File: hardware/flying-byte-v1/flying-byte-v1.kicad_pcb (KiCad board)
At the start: 4 copper layers, 0 parts

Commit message: feat: Add the net classes colors and initialize pcb with parts
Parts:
- added C1: 4u7, Capacitor_SMD:C_0603_1608Metric, F.Cu at (142.5, 90.8)
- added C10: 4u7, Capacitor_SMD:C_0603_1608Metric, F.Cu at (142.5, 98.4)
- added C11: 100n, Capacitor_SMD:C_0402_1005Metric, F.Cu at (129.7, 96.7)
- added C12: 100n, Capacitor_SMD:C_0402_1005Metric, F.Cu at (129.7, 98.7)
- added C13: 100n, Capacitor_SMD:C_0402_1005Metric, F.Cu at (129.7, 100.6)
- added C14: 4u7, Capacitor_SMD:C_0603_1608Metric, F.Cu at (142.5, 100.9)
- added C15: 0p8, Capacitor_SMD:C_0402_1005Metric, F.Cu at (129.7, 102.6)
- added C16: 0p3, Capacitor_SMD:C_0402_1005Metric, F.Cu at (132.6, 94.7)
- added C17: 10p, Capacitor_SMD:C_0402_1005Metric, F.Cu at (132.6, 96.7)
- added C18: 10p, Capacitor_SMD:C_0402_1005Metric, F.Cu at (132.6, 98.7)
- added C19: 100n, Capacitor_SMD:C_0402_1005Metric, F.Cu at (132.6, 100.6)
- added C2: 4u7, Capacitor_SMD:C_0603_1608Metric, F.Cu at (142.5, 93.3)
- added C3: 4u7, Capacitor_SMD:C_0603_1608Metric, F.Cu at (142.5, 95.9)
- added C4: 100n, Capacitor_SMD:C_0402_1005Metric, F.Cu at (126.8, 94.7)
- added C5: 100n, Capacitor_SMD:C_0402_1005Metric, F.Cu at (126.8, 96.7)
- added C6: 100n, Capacitor_SMD:C_0402_1005Metric, F.Cu at (126.8, 98.7)
- added C7: 100n, Capacitor_SMD:C_0402_1005Metric, F.Cu at (126.8, 100.6)
- added C8: 100n, Capacitor_SMD:C_0402_1005Metric, F.Cu at (126.8, 102.6)
- added C9: 100n, Capacitor_SMD:C_0402_1005Metric, F.Cu at (129.7, 94.7)
- added D1: LED, LED_SMD:LED_0402_1005Metric, F.Cu at (151.6, 95.8)
- added D2: LED, LED_SMD:LED_0402_1005Metric, F.Cu at (151.6, 97.8)
- added FLT1: DLF162500LT-5028A1, flying-byte-v1-pcb-footprints:DLF162500LT-5028A1, F.Cu at (146.3, 102.0)
- added J1: Conn_Coaxial, Connector_Coaxial:U.FL_Hirose_U.FL-R-SMT-1_Vertical, F.Cu at (147.1, 97.9)
- added J2: Conn_ARM_SWD_TagConnect_TC2030, Connector:Tag-Connect_TC2030-IDC-FP_2x03_P1.27mm_Vertical, F.Cu at (141.9, 79.2)
- added J3: USB_C_Receptacle_USB2.0, Connector_USB:USB_C_Receptacle_GCT_USB4105-xx-A_16P_TopMnt_Horizontal, F.Cu at (131.3, 79.7)
- added J4: Conn_01x04, Connector_Molex:Molex_PicoBlade_53047-0410_1x04_P1.25mm_Vertical, F.Cu at (147.1, 92.7)
- added L1: 10n, Inductor_SMD:L_0402_1005Metric, F.Cu at (136.2, 85.4)
- added L2: 10u, Inductor_SMD:L_0805_2012Metric, F.Cu at (137.0, 101.4)
- added L3: 2n7, Inductor_SMD:L_0402_1005Metric, F.Cu at (136.2, 87.4)
- added R1: 220R, Resistor_SMD:R_0402_1005Metric, F.Cu at (136.2, 89.4)
- added R2: 220R, Resistor_SMD:R_0402_1005Metric, F.Cu at (136.2, 91.4)
- added R3: 220R, Resistor_SMD:R_0402_1005Metric, F.Cu at (136.2, 93.4)
- added R4: 220R, Resistor_SMD:R_0402_1005Metric, F.Cu at (136.2, 95.4)
- added R5: 5k1, Resistor_SMD:R_0402_1005Metric, F.Cu at (139.1, 85.4)
- added R6: 5k1, Resistor_SMD:R_0402_1005Metric, F.Cu at (139.1, 87.4)
- added R7: 0, Resistor_SMD:R_0402_1005Metric, F.Cu at (139.1, 89.4)
- added R8: 5k1, Resistor_SMD:R_0402_1005Metric, F.Cu at (139.1, 91.4)
- added R9: 220R, Resistor_SMD:R_0402_1005Metric, F.Cu at (139.1, 93.4)
- added SW1: SW_Push, Button_Switch_SMD:SW_SPST_CK_RS282G05A3, F.Cu at (145.9, 87.0)
- added U1: STM32WB55CEU6, Package_DFN_QFN:QFN-48-1EP_7x7mm_P0.5mm_EP5.6x5.6mm, F.Cu at (130.1, 89.1)
- added U2: USBLC6-2SC6_MOD, Package_TO_SOT_SMD:SOT-23-6, F.Cu at (148.7, 76.7)
- added U3: MIC5365-3.3YD5, Package_TO_SOT_SMD:SOT-23-5, F.Cu at (148.7, 81.1)
- added X1: 32MHz, Crystal:Crystal_SMD_2016-4Pin_2.0x1.6mm, F.Cu at (136.6, 98.2)
- added X2: 32kHz768, Crystal:Crystal_SMD_2012-2Pin_2.0x1.2mm, F.Cu at (151.7, 100.2)

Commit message: feat: Add the initial layout
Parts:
- J4: footprint Connector_Molex:Molex_PicoBlade_53047-0410_1x04_P1.25mm_Vertical -> Connector_Molex:Molex_PicoBlade_53048-0410_1x04_P1.25mm_Horizontal
- moved J4 49.3 mm to (97.9, 96.6), turned to -90 degrees
- moved D1 44.4 mm to (107.3, 99.0)
- moved U3 44.0 mm to (106.8, 94.5), turned to -90 degrees
- moved U2 43.3 mm to (106.8, 87.4)
- moved R5 42.6 mm to (97.2, 93.4), turned to 180 degrees
- moved R6 42.3 mm to (97.2, 81.3), turned to 180 degrees
- moved C2 36.0 mm to (106.8, 97.5), turned to 180 degrees
- moved C1 35.7 mm to (106.8, 91.5), turned to 180 degrees
- moved J3 34.9 mm to (97.2, 87.3), turned to -90 degrees
- moved R1 30.8 mm to (107.3, 100.2), turned to 180 degrees
- moved J2 28.4 mm to (115.3, 89.1), turned to -90 degrees
- moved X2 26.3 mm to (125.7, 96.0), turned to 180 degrees
- moved C10 25.2 mm to (123.8, 81.5), turned to 180 degrees
- moved SW1 23.4 mm to (126.4, 100.0)
- moved C14 22.4 mm to (128.5, 83.4)
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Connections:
- net Net-(C17-Pad1) renamed /LSE_OUT_R
- net Net-(J4-Pin_2) renamed /UART_RXC
- net Net-(J4-Pin_3) renamed /UART_TXC
- net Net-(R9-Pad2) renamed /BOOT0_SW

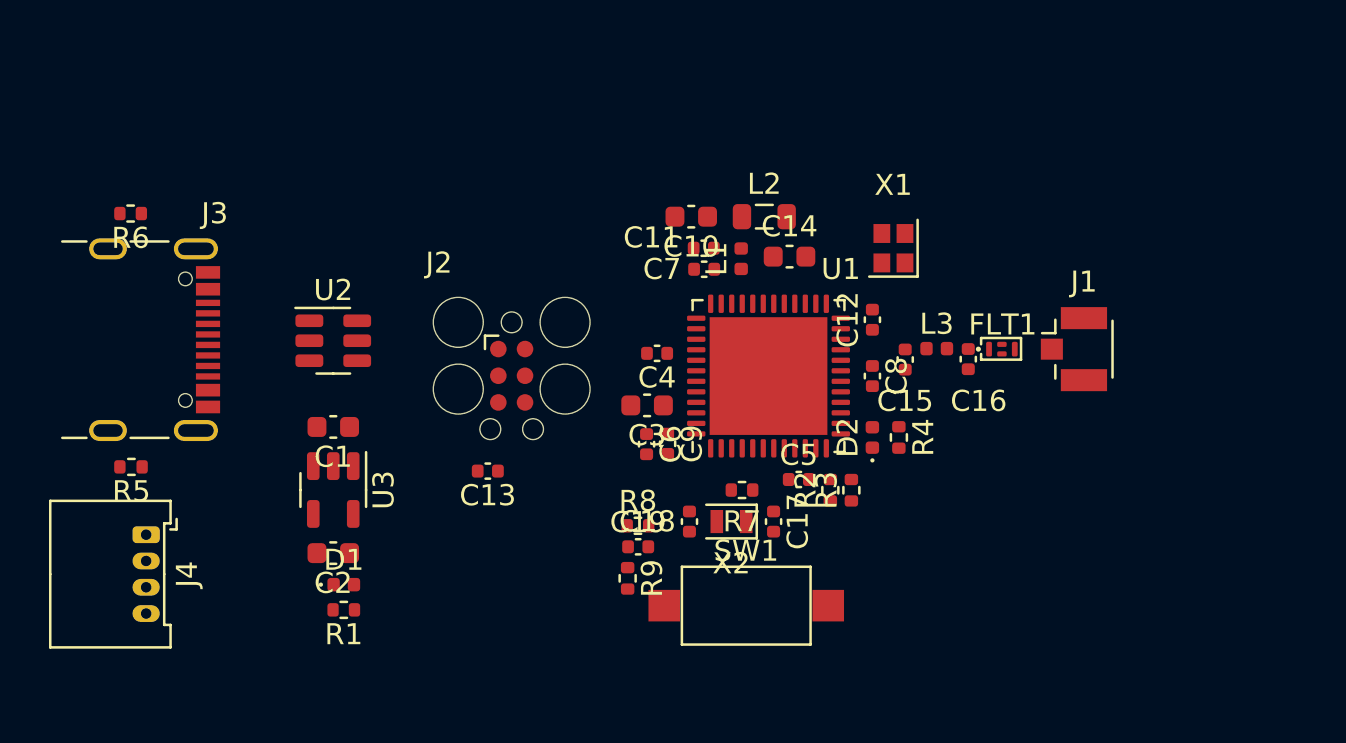
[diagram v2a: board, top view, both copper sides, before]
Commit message: feat: Add outline, mounting holes and fiducial markers
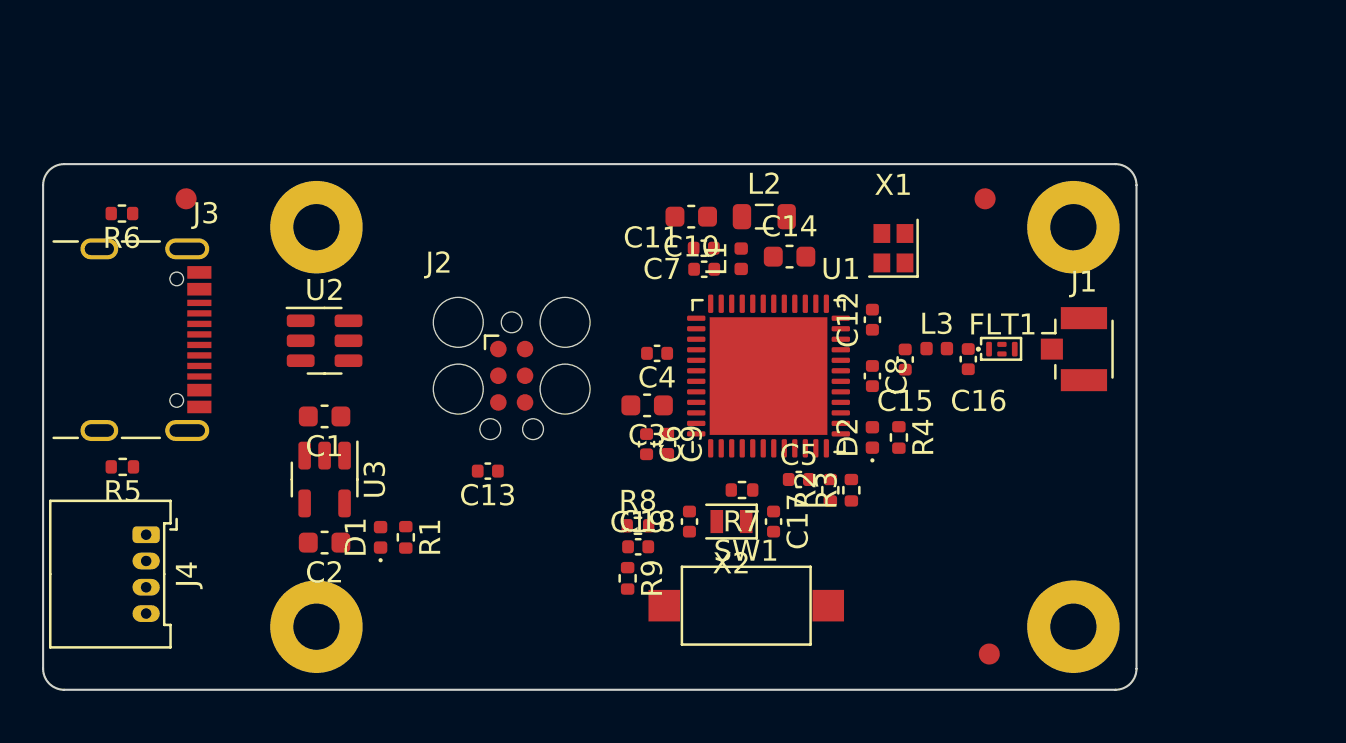
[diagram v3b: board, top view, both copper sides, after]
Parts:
- added FM1: Fiducial, Fiducial:Fiducial_1mm_Mask2mm, F.Cu at (138.0, 102.3)
- added FM2: Fiducial, Fiducial:Fiducial_1mm_Mask2mm, F.Cu at (137.8, 80.7)
- added FM3: Fiducial, Fiducial:Fiducial_1mm_Mask2mm, F.Cu at (99.8, 80.7)
- added H1: MountingHole_Pad, MountingHole:MountingHole_2.2mm_M2_Pad, F.Cu at (142.0, 82.0)
- added H2: MountingHole_Pad, MountingHole:MountingHole_2.2mm_M2_Pad, F.Cu at (142.0, 101.0)
- added H3: MountingHole_Pad, MountingHole:MountingHole_2.2mm_M2_Pad, F.Cu at (106.0, 82.0)
- added H4: MountingHole_Pad, MountingHole:MountingHole_2.2mm_M2_Pad, F.Cu at (106.0, 101.0)
- moved R1 4.54 mm to (110.2, 96.8), turned to -90 degrees
- moved D1 2.85 mm to (109.0, 96.8), turned to 90 degrees
- moved C1 0.65 mm to (106.4, 91.0)
- moved C2 0.65 mm to (106.4, 97.0)
- moved U3 0.65 mm to (106.4, 94.0)
- moved R5 0.41 mm to (96.8, 93.4)
- moved J3 0.41 mm to (96.8, 87.3)
- moved R6 0.41 mm to (96.8, 81.3)
- moved U2 0.41 mm to (106.4, 87.4)
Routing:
- added copper zone on In1.Cu, net GND
- added copper zone on In2.Cu, net GND
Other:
- board outline added: 52 x 25 mm

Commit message: feat: PCB routing #1
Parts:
- moved C19 12.7 mm to (133.1, 102.0)
- moved R8 12.7 mm to (133.1, 101.0)
- moved R9 11.1 mm to (131.5, 101.5), turned to 90 degrees
- moved R2 0.93 mm to (129.5, 94.3)
- moved R3 0.93 mm to (130.5, 94.3)
- moved C5 0.67 mm to (128.3, 94.3), turned to -90 degrees
- moved C17 0.64 mm to (127.2, 96.4)
- moved C18 0.64 mm to (123.2, 96.4)
- moved R7 0.64 mm to (125.7, 94.9)
- moved X2 0.64 mm to (125.2, 96.4)
- moved C4 0.60 mm to (121.6, 88.1)
- moved SW1 0.60 mm to (125.9, 100.2), turned to 180 degrees
- moved C13 0.29 mm to (113.9, 93.6)
- moved J2 0.28 mm to (115.0, 89.1)
- moved C12 0.16 mm to (132.6, 86.4)
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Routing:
- net /USB_D-: track 0.00 -> 16.8 mm
- net /USB_D+: track 0.00 -> 16.4 mm
- net /SWD_NRST: track 0.00 -> 15.9 mm, vias 0 -> 2
- net /BOOT0: track 0.00 -> 14.8 mm, vias 0 -> 2
- net /SWD_DIO: track 0.00 -> 12.0 mm
- net /SWD_TRC: track 0.00 -> 10.3 mm
- net /SWD_CLK: track 0.00 -> 9.29 mm
- net /LSE_IN: track 0.00 -> 5.65 mm
- net /HSE_OUT: track 0.00 -> 5.21 mm
- net /HSE_IN: track 0.00 -> 5.06 mm
- net /RF: track 0.00 -> 4.10 mm
- net /LSE_OUT_R: track 0.00 -> 3.13 mm
- net /LSE_OUT: track 0.00 -> 2.57 mm
- net /RF_MATCH: track 0.00 -> 2.03 mm
- net /RF_ANT: track 0.00 -> 1.76 mm
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- added copper zone on F.Cu, net /SMPS_VFB

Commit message: feat: PCB routing #2
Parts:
- turned U2 to 0 degrees
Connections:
- U2 pad 1: /USBC_D+ -> /USBC_D-
- U2 pad 3: /USBC_D- -> /USBC_D+
- U2 pad 4: /USB_D- -> /USB_D+
- U2 pad 6: /USB_D+ -> /USB_D-
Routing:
- net /USBC_D+: track 0.00 -> 8.59 mm
- net /USBC_D-: track 0.00 -> 8.10 mm
- net /USBC_CC1: track 0.00 -> 6.84 mm
- net /USBC_CC2: track 0.00 -> 6.38 mm
- net /USB_D+: track 16.4 -> 21.4 mm
- net /USB_D-: track 16.8 -> 20.7 mm
- net GND: vias 37 -> 39
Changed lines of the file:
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@@
   )
   (footprint "Package_TO_SOT_SMD:SOT-23-6" (layer "F.Cu")
-    (at 106.3875 87.4 180)
+    (at 106.3875 87.4)
     (descr "SOT, 6 Pin (https://www.jedec.org/sites/default/files/docs/Mo-178c.PDF variant AB), generated with kicad-footprint-generator ipc_gullwing_generator.py")
     (tags "SOT TO_SOT_SMD")
@@
     (fp_line (start 0.8 1.45) (end -0.8 1.45)
       (stroke (width 0.1) (type solid)) (layer "F.Fab"))
-    (pad "1" smd roundrect (at -1.1375 -0.95 180) (size 1.325 0.6) (layers "F.Cu" "F.Paste" "F.Mask") (roundrect_rratio 0.25)
+    (pad "1" smd roundrect (at -1.1375 -0.95) (size 1.325 0.6) (layers "F.Cu" "F.Paste" "F.Mask") (roundrect_rratio 0.25)
+      (net 20 "/USBC_D-") (pinfunction "I/O1") (pintype "passive"))
+    (pad "2" smd roundrect (at -1.1375 0) (size 1.325 0.6) (layers "F.Cu" "F.Paste" "F.Mask") (roundrect_rratio 0.25)
+      (net 2 "GND") (pinfunction "GND") (pintype "passive"))
+    (pad "3" smd roundrect (at -1.1375 0.95) (size 1.325 0.6) (layers "F.Cu" "F.Paste" "F.Mask") (roundrect_rratio 0.25)
       (net 19 "/USBC_D+") (pinfunction "I/O1") (pintype "passive"))
-    (pad "2" smd roundrect (at -1.1375 0 180) (size 1.325 0.6) (layers "F.Cu" "F.Paste" "F.Mask") (roundrect_rratio 0.25)
-      (net 2 "GND") (pinfunction "GND") (pintype "passive"))
-    (pad "3" smd roundrect (at -1.1375 0.95 180) (size 1.325 0.6) (layers "F.Cu" "F.Paste" "F.Mask") (roundrect_rratio 0.25)
-      (net 20 "/USBC_D-") (pinfunction "I/O1") (pintype "passive"))
-    (pad "4" smd roundrect (at 1.1375 0.95 180) (size 1.325 0.6) (layers "F.Cu" "F.Paste" "F.Mask") (roundrect_rratio 0.25)
+    (pad "4" smd roundrect (at 1.1375 0.95) (size 1.325 0.6) (layers "F.Cu" "F.Paste" "F.Mask") (roundrect_rratio 0.25)
+      (net 51 "/USB_D+") (pinfunction "I/O2") (pintype "passive"))
+    (pad "5" smd roundrect (at 1.1375 0) (size 1.325 0.6) (layers "F.Cu" "F.Paste" "F.Mask") (roundrect_rratio 0.25)
+      (net 1 "+5V") (pinfunction "VBUS") (pintype "passive"))
+    (pad "6" smd roundrect (at 1.1375 -0.95) (size 1.325 0.6) (layers "F.Cu" "F.Paste" "F.Mask") (roundrect_rratio 0.25)
       (net 50 "/USB_D-") (pinfunction "I/O2") (pintype "passive"))
-    (pad "5" smd roundrect (at 1.1375 0 180) (size 1.325 0.6) (layers "F.Cu" "F.Paste" "F.Mask") (roundrect_rratio 0.25)
-      (net 1 "+5V") (pinfunction "VBUS") (pintype "passive"))
-    (pad "6" smd roundrect (at 1.1375 -0.95 180) (size 1.325 0.6) (layers "F.Cu" "F.Paste" "F.Mask") (roundrect_rratio 0.25)
-      (net 51 "/USB_D+") (pinfunction "I/O2") (pintype "passive"))
     (model "${KICAD6_3DMODEL_DIR}/Package_TO_SOT_SMD.3dshapes/SOT-23-6.wrl"
       (offset (xyz 0 0 0))
@@
   (via (at 142.5 85) (size 0.7) (drill 0.3) (layers "F.Cu" "B.Cu") (free) (net 2))
   (via (at 104.45 91.45) (size 0.7) (drill 0.3) (layers "F.Cu" "B.Cu") (free) (net 2))
+  (via (at 103.91 87.4) (size 0.7) (drill 0.3) (layers "F.Cu" "B.Cu") (free) (net 2))
   (via (at 127.22 97.71) (size 0.7) (drill 0.3) (layers "F.Cu" "B.Cu") (free) (net 2))
   (via (at 131.86 83.9) (size 0.7) (drill 0.3) (layers "F.Cu" "B.Cu") (free) (net 2))
@@
   (via (at 110.25 95.35) (size 0.7) (drill 0.3) (layers "F.Cu" "B.Cu") (free) (net 2))
   (via (at 121.8 82) (size 0.7) (drill 0.3) (layers "F.Cu" "B.Cu") (free) (net 2))
+  (via (at 133.5 93.8) (size 0.7) (drill 0.3) (layers "F.Cu" "B.Cu") (free) (net 2))
   (via (at 142.5 90.6) (size 0.7) (drill 0.3) (layers "F.Cu" "B.Cu") (free) (net 2))
   (via (at 123 83) (size 0.7) (drill 0.3) (layers "F.Cu" "B.Cu") (free) (net 2))
@@
   (segment (start 118.275 91.425) (end 117.025 91.425) (width 0.17) (layer "F.Cu") (net 17))
   (segment (start 119.455 89.33) (end 119.45 89.325) (width 0.17) (layer "F.Cu") (net 17))
+  (segment (start 99.1 86.1) (end 97.26 84.26) (width 0.25) (layer "F.Cu") (net 18))
+  (segment (start 97.26 84.26) (end 97.26 81.35) (width 0.25) (layer "F.Cu") (net 18))
+  (segment (start 100.43 86.1) (end 99.1 86.1) (width 0.25) (layer "F.Cu") (net 18))
+  (segment (start 100.43 87.1) (end 101.292501 87.1) (width 0.22) (layer "F.Cu") (net 19))
+  (segment (start 103.81 88.35) (end 105.25 88.35) (width 0.22) (layer "F.Cu") (net 19))
+  (segment (start 102.978456 88.1) (end 103.169228 87.909228) (width 0.22) (layer "F.Cu") (net 19))
+  (segment (start 101.342501 87.05) (end 102.624228 87.05) (width 0.22) (layer "F.Cu") (net 19))
+  (segment (start 102.624228 87.05) (end 103.169228 87.595) (width 0.22) (layer "F.Cu") (net 19))
+  (segment (start 103.169228 87.595) (end 103.169228 87.909228) (width 0.22) (layer "F.Cu") (net 19))
+  (segment (start 101.292501 87.1) (end 101.342501 87.05) (width 0.22) (layer "F.Cu") (net 19))
+  (segment (start 102.978456 88.1) (end 103.094228 87.984228) (width 0.22) (layer "F.Cu") (net 19))
+  (segment (start 103.094228 87.984228) (end 103.444228 87.984228) (width 0.22) (layer "F.Cu") (net 19))
+  (segment (start 100.43 88.1) (end 102.978456 88.1) (width 0.22) (layer "F.Cu") (net 19))
+  (segment (start 103.444228 87.984228) (end 103.81 88.35) (width 0.22) (layer "F.Cu") (net 19))
+  (segment (start 100.43 86.6) (end 101.292501 86.6) (width 0.22) (layer "F.Cu") (net 20))
+  (segment (start 101.292501 86.6) (end 101.352501 86.66) (width 0.22) (layer "F.Cu") (net 20))
+  (segment (start 102.765772 86.66) (end 102.975772 86.45) (width 0.22) (layer "F.Cu") (net 20))
+  (segment (start 102.975772 86.45) (end 105.25 86.45) (width 0.22) (layer "F.Cu") (net 20))
+  (segment (start 99.23 87.4) (end 99.23 86.8) (width 0.22) (layer "F.Cu") (net 20))
+  (segment (start 99.43 86.6) (end 100.43 86.6) (width 0.22) (layer "F.Cu") (net 20))
+  (segment (start 100.43 87.6) (end 99.43 87.6) (width 0.22) (layer "F.Cu") (net 20))
+  (segment (start 101.352501 86.66) (end 102.765772 86.66) (width 0.22) (layer "F.Cu") (net 20))
+  (segment (start 99.43 87.6) (end 99.23 87.4) (width 0.22) (layer "F.Cu") (net 20))
+  (segment (start 99.23 86.8) (end 99.43 86.6) (width 0.22) (layer "F.Cu") (net 20))
+  (segment (start 100.43 89.1) (end 99.1 89.1) (width 0.25) (layer "F.Cu") (net 22))
+  (segment (start 97.2975 90.9025) (end 97.2975 93.4) (width 0.25) (layer "F.Cu") (net 22))
+  (segment (start 99.1 89.1) (end 97.2975 90.9025) (width 0.25) (layer "F.Cu") (net 22))
   (segment (start 126.25 84.675) (end 126.25 83.985) (width 0.5) (layer "F.Cu") (net 26))
   (segment (start 126.25 85.6425) (end 126.25 84.85) (width 0.25) (layer "F.Cu") (net 26))
@@
   (segment (start 131.2 83.2) (end 131.2 84.1) (width 0.17) (layer "F.Cu") (net 43))
   (segment (start 132.1 82.3) (end 131.2 83.2) (width 0.17) (layer "F.Cu") (net 43))
-  (segment (start 122.860772 86.385) (end 119.560772 83.085) (width 0.22) (layer "F.Cu") (net 50))
-  (segment (start 123.406249 86.33) (end 123.351249 86.385) (width 0.22) (layer "F.Cu") (net 50))
-  (segment (start 110.619228 83.085) (end 109.262114 84.442114) (width 0.22) (layer "F.Cu") (net 50))
+  (segment (start 119.560772 83.085) (end 110.619228 83.085) (width 0.22) (layer "F.Cu") (net 50))
+  (segment (start 110.619228 83.085) (end 109.904888 83.79934) (width 0.22) (layer "F.Cu") (net 50))
+  (segment (start 109.524228 86.45) (end 107.525 86.45) (width 0.22) (layer "F.Cu") (net 50))
+  (segment (start 109.904888 83.79934) (end 109.904888 86.06934) (width 0.22) (layer "F.Cu") (net 50))
+  (segment (start 109.904888 86.06934) (end 109.524228 86.45) (width 0.22) (layer "F.Cu") (net 50))
   (segment (start 123.351249 86.385) (end 122.860772 86.385) (width 0.22) (layer "F.Cu") (net 50))
   (segment (start 124.0625 86.33) (end 123.406249 86.33) (width 0.22) (layer "F.Cu") (net 50))
-  (segment (start 119.560772 83.085) (end 110.619228 83.085) (width 0.22) (layer "F.Cu") (net 50))
+  (segment (start 123.406249 86.33) (end 123.351249 86.385) (width 0.22) (layer "F.Cu") (net 50))
+  (segment (start 122.860772 86.385) (end 119.560772 83.085) (width 0.22) (layer "F.Cu") (net 50))
+  (segment (start 108.45 88.35) (end 107.525 88.35) (width 0.22) (layer "F.Cu") (net 51))
   (segment (start 119.399228 83.475) (end 110.780772 83.475) (width 0.22) (layer "F.Cu") (net 51))
+  (segment (start 110.294888 83.960884) (end 110.294888 86.505112) (width 0.22) (layer "F.Cu") (net 51))
+  (segment (start 123.351249 86.775) (end 122.699228 86.775) (width 0.22) (layer "F.Cu") (net 51))
+  (segment (start 110.294888 86.505112) (end 108.45 88.35) (width 0.22) (layer "F.Cu") (net 51))
+  (segment (start 110.780772 83.475) (end 110.294888 83.960884) (width 0.22) (layer "F.Cu") (net 51))
   (segment (start 123.406249 86.83) (end 123.351249 86.775) (width 0.22) (layer "F.Cu") (net 51))
-  (segment (start 123.351249 86.775) (end 122.699228 86.775) (width 0.22) (layer "F.Cu") (net 51))
   (segment (start 122.699228 86.775) (end 119.399228 83.475) (width 0.22) (layer "F.Cu") (net 51))
-  (segment (start 110.780772 83.475) (end 109.537886 84.717886) (width 0.22) (layer "F.Cu") (net 51))
   (segment (start 124.0625 86.83) (end 123.406249 86.83) (width 0.22) (layer "F.Cu") (net 51))
   (zone (net 5) (net_name "/SMPS_VFB") (layer "F.Cu") (hatch edge 0.5)

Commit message: feat: PCB routing #3
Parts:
- moved C13 4.96 mm to (118.8, 94.0), turned to -90 degrees
- moved C5 0.73 mm to (128.3, 95.1)
- moved R8 0.66 mm to (132.8, 101.6)
- moved SW1 0.66 mm to (125.7, 100.9)
- moved C17 0.66 mm to (127.0, 97.0)
- moved C18 0.66 mm to (123.0, 97.0)
- moved R7 0.66 mm to (125.5, 95.5)
- moved X2 0.66 mm to (125.0, 97.0)
- moved C19 0.66 mm to (132.9, 102.6)
- moved R9 0.66 mm to (131.3, 102.2)
- moved C1 0.23 mm to (106.4, 90.8)
- moved C2 0.23 mm to (106.4, 96.8)
- moved D1 0.23 mm to (109.1, 96.5)
- moved R1 0.23 mm to (110.3, 96.5)
- moved U3 0.23 mm to (106.4, 93.8)
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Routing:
- net /UART_RXC: track 0.00 -> 35.6 mm, vias 0 -> 2
- net /UART_TXC: track 0.00 -> 35.5 mm, vias 0 -> 2
- net +5V: track 0.00 -> 24.2 mm
- net +3V3: track 1.37 -> 20.9 mm, vias 6 -> 11
- net /SWD_NRST: track 15.9 -> 29.6 mm
- net GND: track 0.00 -> 7.91 mm, vias 39 -> 146
- net /BOOT0_SW: track 0.00 -> 2.41 mm
- net /BOOT0: track 14.8 -> 17.2 mm
- net /LED_A: track 0.00 -> 2.21 mm
- net /LED_K: track 0.00 -> 1.27 mm
- net /LSE_OUT: track 2.57 -> 3.28 mm
- net /LSE_IN: track 5.65 -> 6.36 mm
- added copper zone on B.Cu, net +3V3
- added copper zone on F.Cu, net +3V3
- added copper zone on F.Cu, net GND
